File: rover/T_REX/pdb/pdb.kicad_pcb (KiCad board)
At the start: 2 copper layers, 96.5 x 97.9 mm, 96 parts, among them J1 Screw_Terminal_01x04, J2 Screw_Terminal_01x02, J3 Screw_Terminal_01x02, Q1 GSF2302, Q2 GSF2302, U3 TJA1050T_CM_118

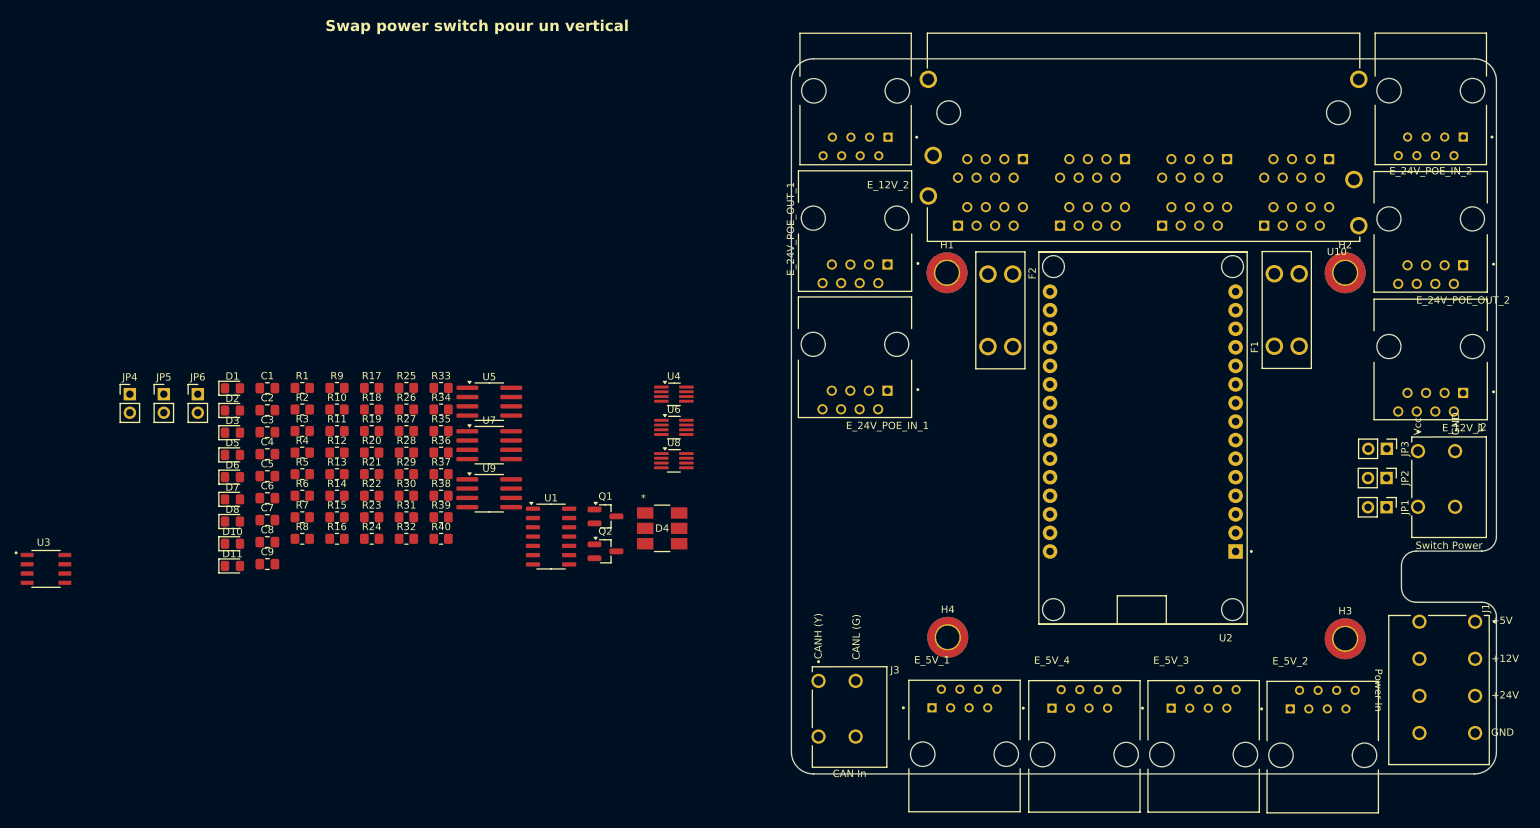
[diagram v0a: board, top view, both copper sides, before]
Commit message: PDB routing
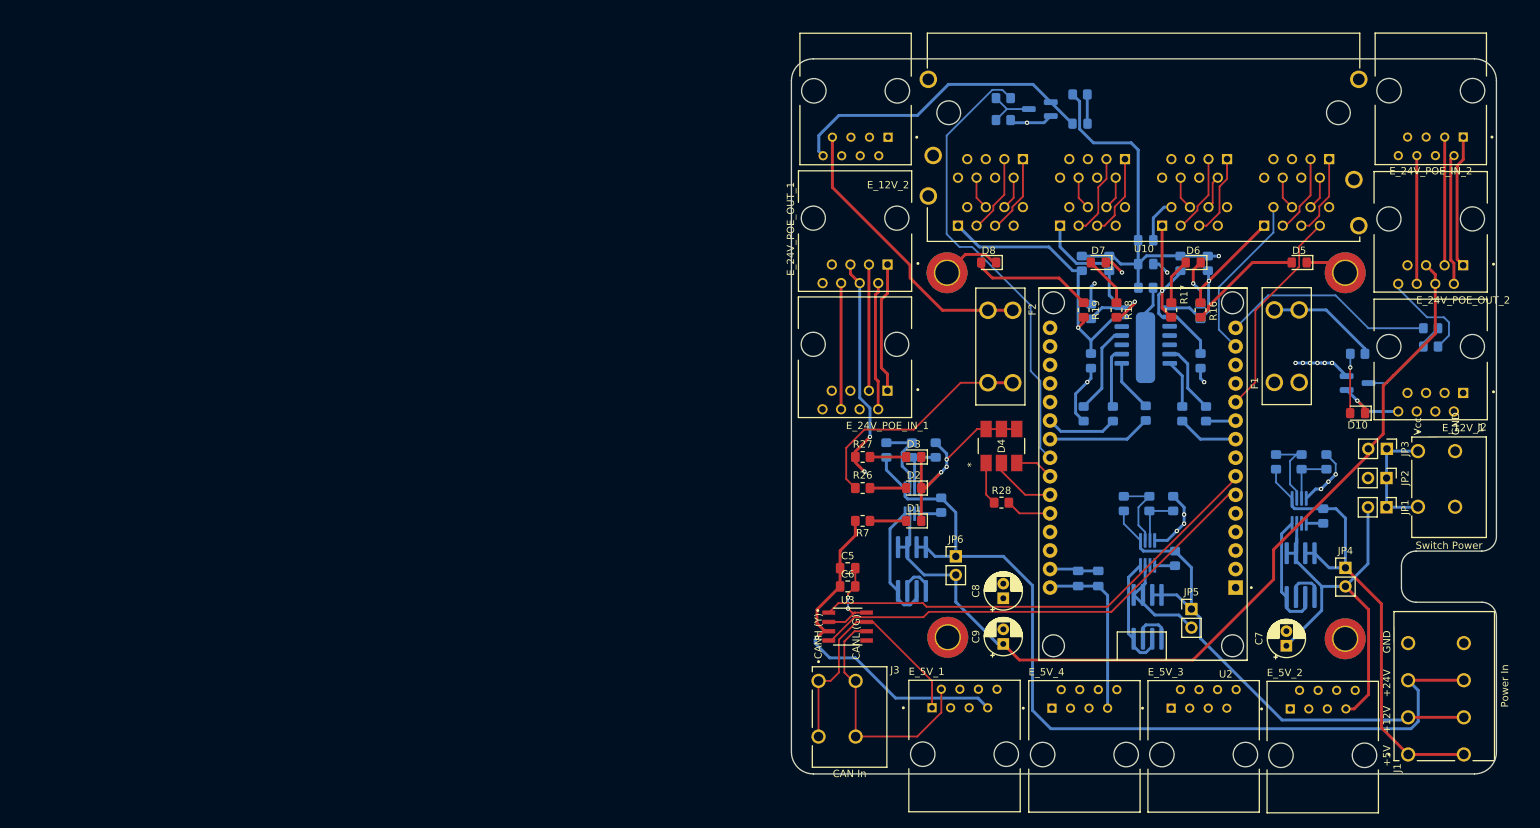
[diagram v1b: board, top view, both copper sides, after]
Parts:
- C1, C2, C3, C4, D11, Q1, Q2, R1, R10, R11, R12, R13, R14, R15, R2, R20, R21, R22, R23, R24, R25, R29, R3, R30, R31, R32, R33, R34, R35, R36, R37, R38, R39, R4, R40, R5, R6, R8, R9, U1, U4, U5, U6, U7, U8, U9: moved to B.Cu
- C7, C8, C9: footprint Capacitor_SMD:C_0805_2012Metric_Pad1.18x1.45mm_HandSolder -> Capacitor_THT:CP_Radial_D5.0mm_P2.00mm
- moved JP4 168.1 mm to (96.8, 89.3)
- moved D10 155.0 mm to (98.5, 68.1), turned to 180 degrees
- moved R2 154.8 mm to (108.5, 56.5)
- moved R1 154.6 mm to (108.5, 59.0)
- moved D5 148.4 mm to (90.5, 47.5), turned to 180 degrees
- moved R3 144.8 mm to (98.5, 60.0)
- moved JP5 143.7 mm to (75.8, 94.9)
- moved C7 140.5 mm to (88.8, 100.0), turned to 90 degrees
- moved D6 134.7 mm to (76.0, 47.5), turned to 180 degrees
- moved D11 130.8 mm to (60.5, 28.5)
- moved R32 126.4 mm to (94.2, 74.8), turned to -90 degrees
- moved R29 125.6 mm to (93.8, 82.2), turned to 90 degrees
- moved D7 122.9 mm to (63.0, 47.5), turned to 180 degrees
- moved R31 122.8 mm to (90.8, 74.8), turned to 90 degrees
- moved C2 122.5 mm to (69.5, 44.5)
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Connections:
- D10 pad 1: GND -> ACC1_LOAD_LOW
- D11 pad 1: GND -> ACC2_LOAD_LOW
- J1 pad 2: +12V_IN -> +12V IN
- J1 pad 3: +24V_IN -> +24V IN
- R3 pad 2: GND -> +12V
- R6 pad 2: GND -> +12V
- U2 pad 11: CAM_SIGN_2 -> PWM_0
- U2 pad 14: CAM_SIGN_3 -> PWM_1
- U2 pad 21: PWM_0 -> CAM_SIGN_3
- U2 pad 22: PWM_1 -> CAM_SIGN_2
- U2 pad 24: LED_R -> LED_B
- U2 pad 26: unconnected-(U2-D14-Pad26) -> LED_R
- U2 pad 28: TXC -> unconnected-(U2-D13-Pad28)
- U2 pad 5: RXC -> unconnected-(U2-D4-Pad5)
- U2 pad 6: unconnected-(U2-RX2-Pad6) -> TXC
- U2 pad 7: unconnected-(U2-TX2-Pad7) -> RXC
- U2 pad 8: LED_B -> unconnected-(U2-D5-Pad8)
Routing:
- net +12V: track 0.00 -> 257.8 mm, vias 0 -> 1
- net +5V: track 0.00 -> 183.7 mm, vias 0 -> 1
- net +24V: track 0.00 -> 177.6 mm, vias 0 -> 2
- net GND: track 0.00 -> 144.0 mm, vias 0 -> 24
- net +24V IN: track 0.00 -> 123.6 mm
- net CANH: track 0.00 -> 88.0 mm
- net CANL: track 0.00 -> 85.3 mm
- net +12V IN: track 0.00 -> 71.3 mm
- net RXC: track 0.00 -> 64.0 mm
- net TXC: track 0.00 -> 63.9 mm
- net +5V IN: track 0.00 -> 63.8 mm
- net ACC2_CONTROL: track 0.00 -> 62.8 mm
- net ACC2_LOAD_LOW: track 0.00 -> 42.9 mm
- net Net-(E_12V_2-Pad7): track 0.00 -> 39.6 mm
- net CAM_POW_3: track 0.00 -> 39.0 mm, vias 0 -> 1
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- added copper zone on In2.Cu, net GND
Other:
- copper layers 2 -> 4
- board text removed: "Swap power switch pour un vertical"

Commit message: fix terminaison
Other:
- board text added: "!ONLY ONE JUMPER!"
- board text added: "12V"
- board text added: "12V Safety Bypass"
- board text added: "24V"
- board text added: "24V Safety Bypass"
- board text added: "5V"
- board text added: "5V Safety Bypass"
- board text added: "CAM A2"
- board text added: "CAM R1M ARM"
- board text added: "CAM R1M AUX"
- board text added: "CAM R1M SCI"
- board text added: "CAN 5V"
- board text added: "CLAQUE SON"
- board text added: "Eth Ordi"
- board text added: "Fuse Claque Son"
- board text added: "Fuse Lights"
- board text added: "Lights"
- board text added: "POE 2.4Ghz"
- board text added: "POE 900Mhz"

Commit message: export pdb step
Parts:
- C1, C4: value 100nf -> 100nF
- C2, C3: value 10uf -> 10uF
- C7, C8, C9: value 100uf -> 100uF
- R35: value 262k -> 62k
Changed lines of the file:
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@@
 			)
 		)
-		(property "Value" "100uf"
+		(property "Value" "100uF"
 			(at 1 3.75 -90)
 			(layer "F.Fab")
@@
 			)
 		)
-		(property "Value" "100uf"
+		(property "Value" "100uF"
 			(at 1 3.75 -90)
 			(layer "F.Fab")
@@
 			)
 		)
-		(property "Value" "100uf"
+		(property "Value" "100uF"
 			(at 1 3.75 -90)
 			(layer "F.Fab")
@@
 			)
 		)
-		(property "Value" "262k"
+		(property "Value" "62k"
 			(at 0 -1.65 90)
 			(layer "B.Fab")
@@
 			)
 		)
-		(property "Value" "100nf"
+		(property "Value" "100nF"
 			(at 0 -1.68 0)
 			(layer "B.Fab")
@@
 			)
 		)
-		(property "Value" "10uf"
+		(property "Value" "10uF"
 			(at 0 -1.68 -90)
 			(layer "B.Fab")
@@
 			)
 		)
-		(property "Value" "10uf"
+		(property "Value" "10uF"
 			(at 0 -1.68 0)
 			(layer "B.Fab")
@@
 			)
 		)
-		(property "Value" "100nf"
+		(property "Value" "100nF"
 			(at 0 -1.68 -90)
 			(layer "B.Fab")
